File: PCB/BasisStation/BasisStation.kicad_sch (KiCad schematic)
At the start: 17 parts, among them J1 Conn_02x05_Odd_Even, J2 Conn_02x03_Odd_Even, U2 ESP32-S3-WROOM-2

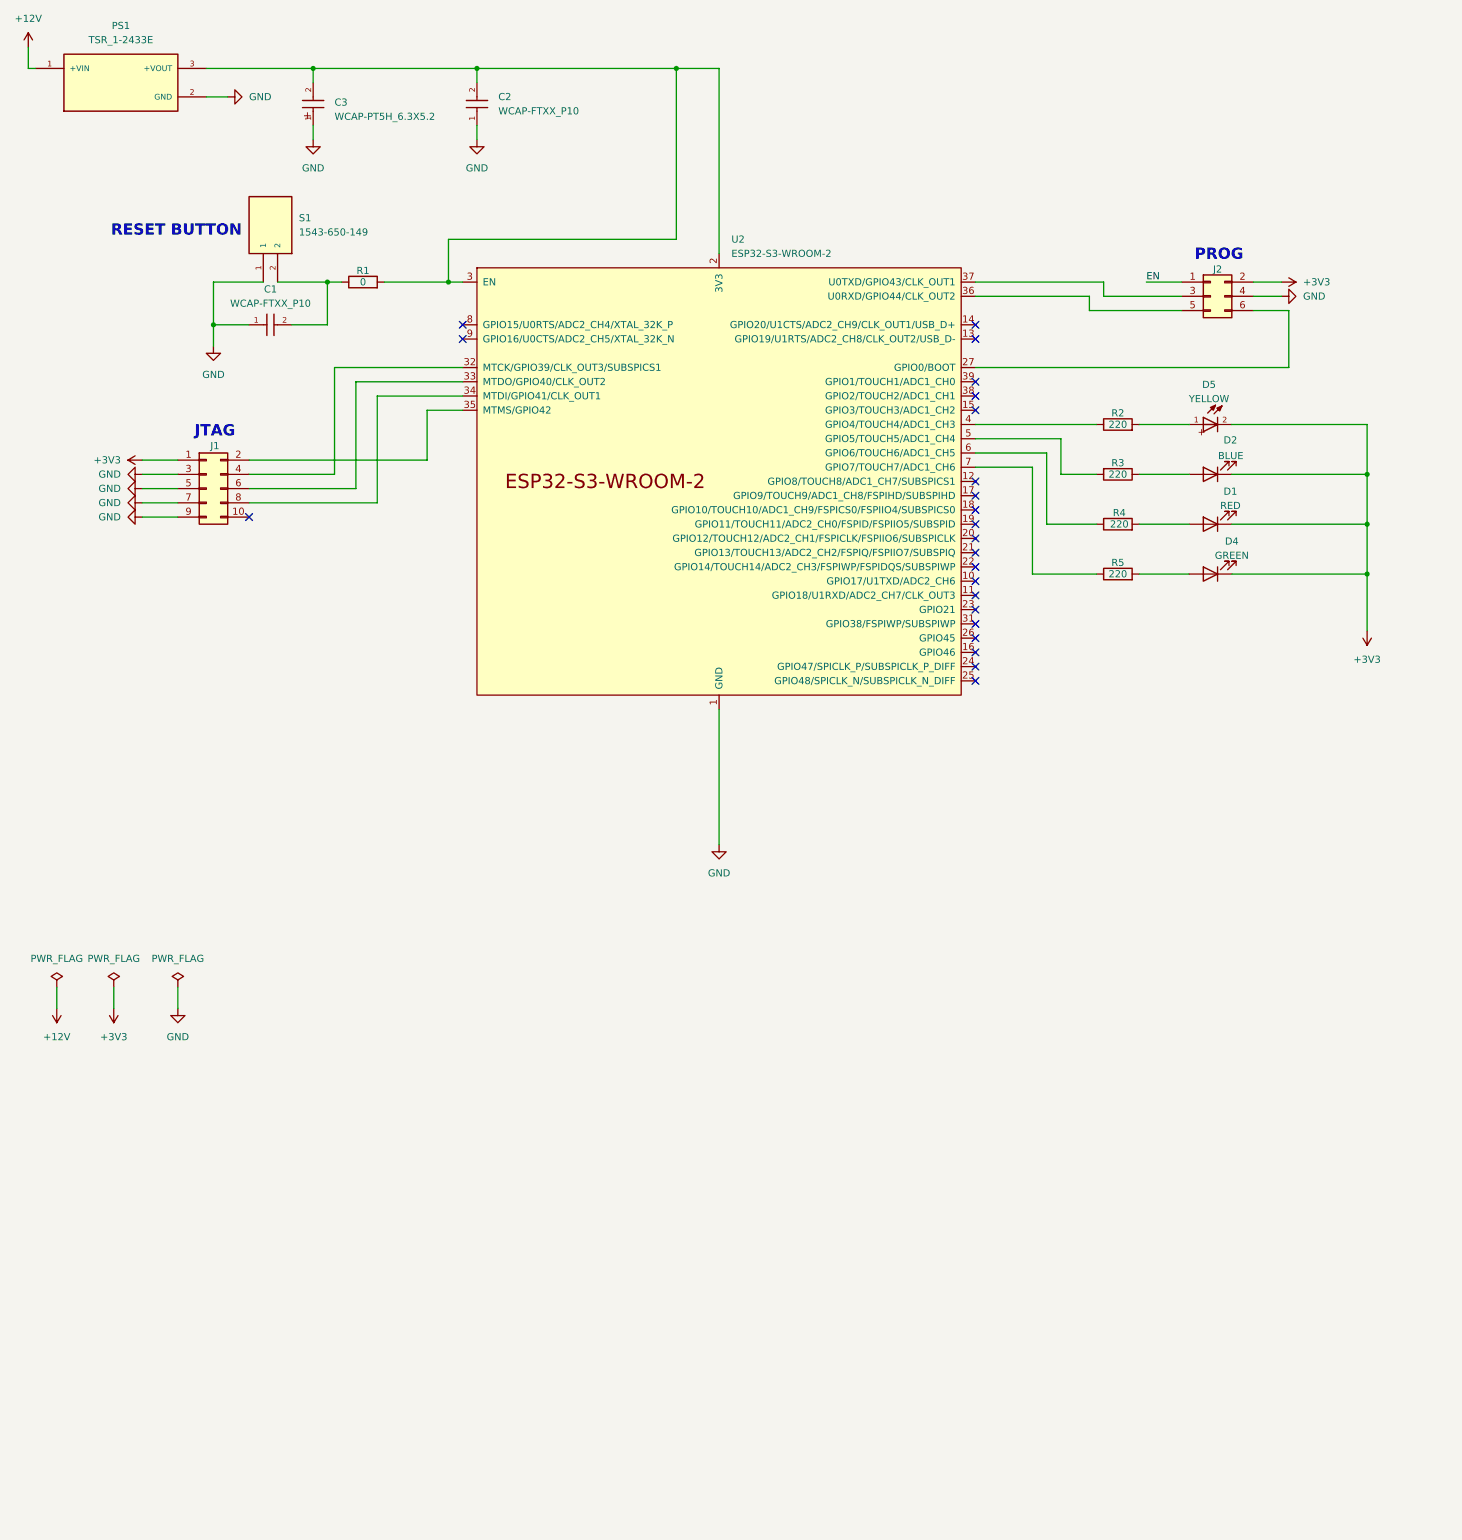
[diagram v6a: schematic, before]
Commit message: microcontroller gewechselt und Layout angepasst
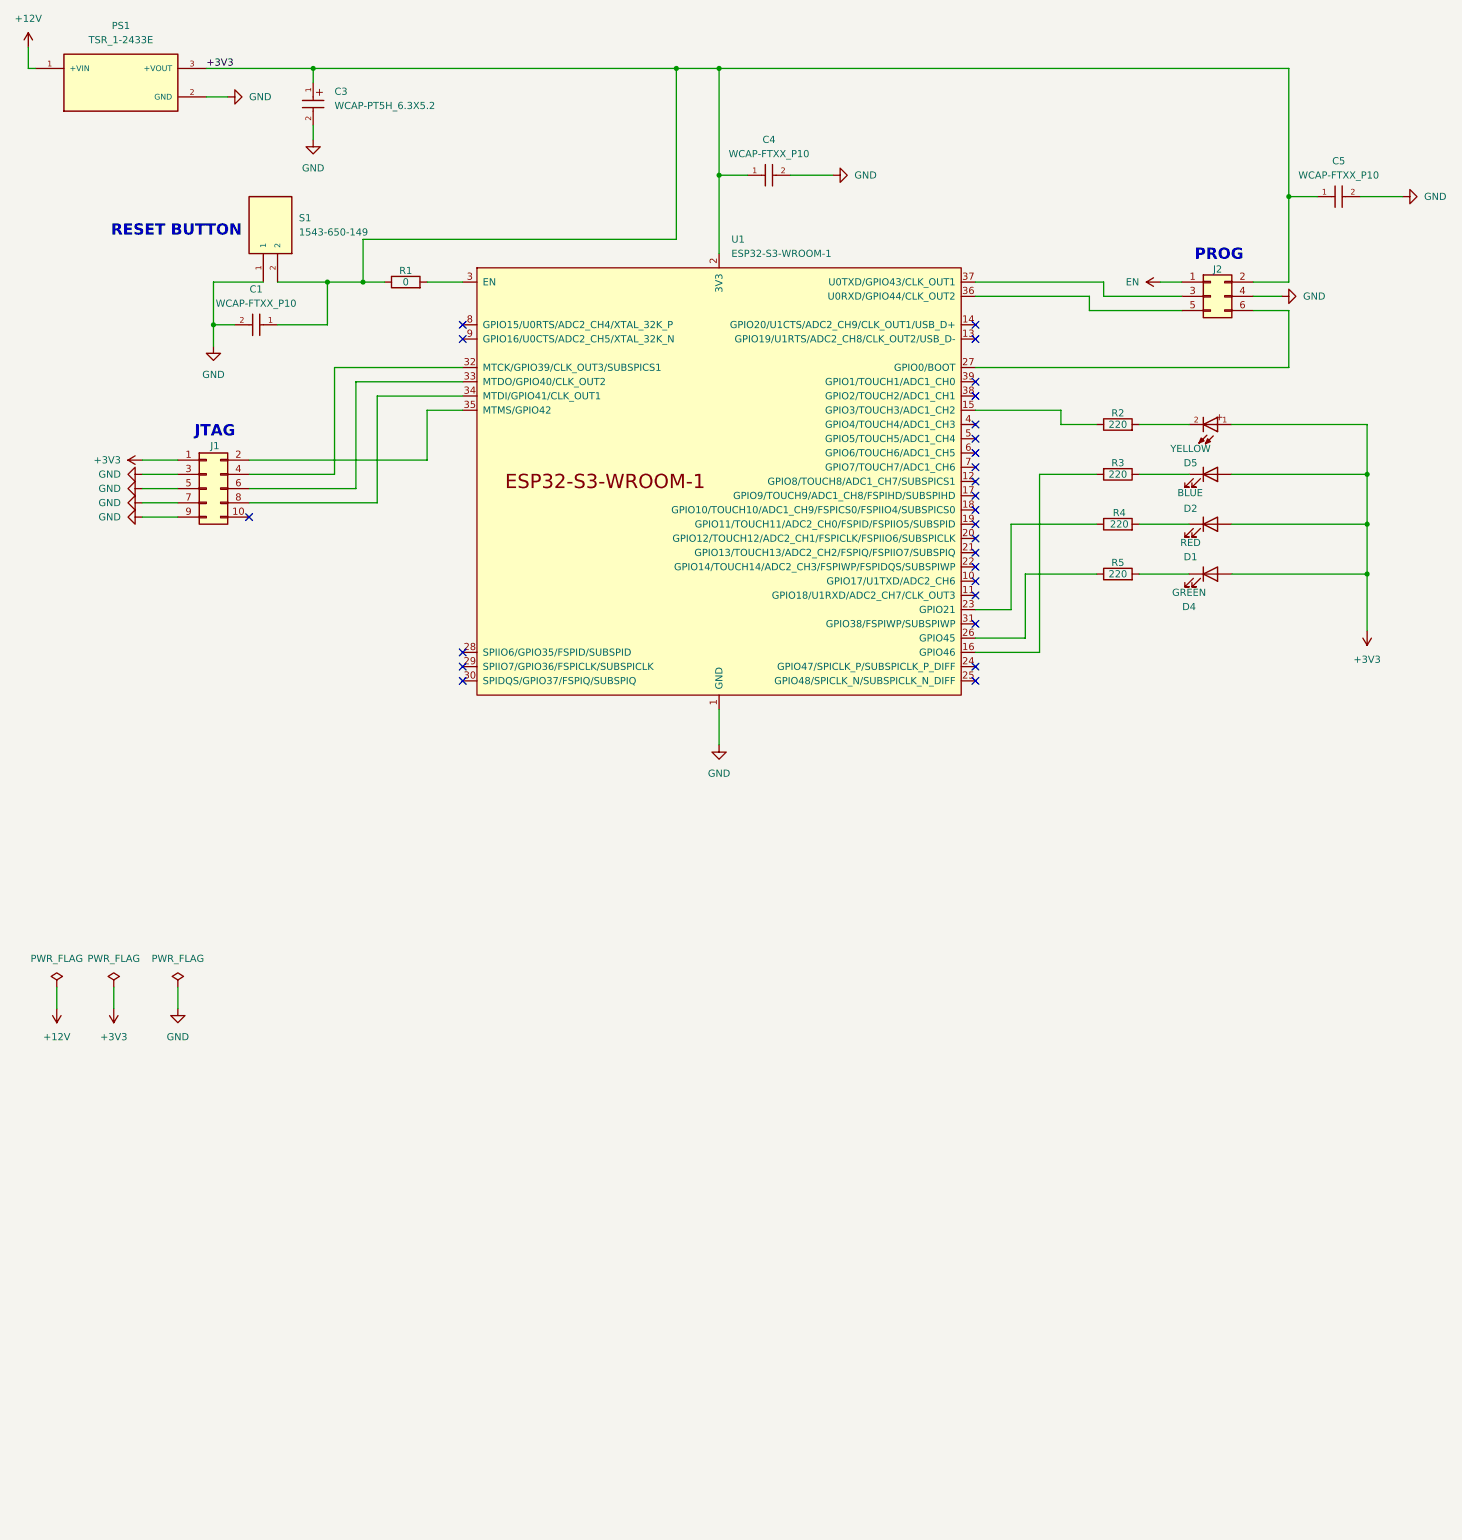
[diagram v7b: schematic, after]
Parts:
- removed C2: WCAP-FTXX_P10, Footprints:WCAP-FTXX_P10L13W7H13, symbol WCAP-FTXX_P10:WCAP-FTXX_P10
- removed U2: ESP32-S3-WROOM-2, Footprints:ESP32-S3-WROOM-2_NEW, symbol PCM_Espressif:ESP32-S3-WROOM-2
- added C4, C5: WCAP-FTXX_P10, Footprints:WCAP-FTXX_P10L13W7H13, symbol WCAP-FTXX_P10:WCAP-FTXX_P10
- added U1: ESP32-S3-WROOM-1, Footprints:ESP32-S3-WROOM-1U, symbol Espressif:ESP32-S3-WROOM-1
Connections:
- net +3V3: now also C1.1, C3.1, D1.2 (A), D2.2 (A), D4.2 (A), D5.1, PS1.3 (+VOUT), R1.1, S1.2, C4.1, C5.1, U1.2 (3V3); no longer D1.1 (K), D2.1 (K), D4.1 (K), D5.2
- net GND: now also C1.2, C3.2, C4.2, C5.2, U1.1 (GND), U1.40 (GND), U1.41 (GND); no longer C1.1, C3.1
- net at R3.1: now also D2.1 (K); no longer D2.2 (A)
- net at R4.1: now also U1.23 (GPIO21)
- net at R4.2: now also D1.1 (K); no longer D1.2 (A)
- net at R5.1: now also U1.26 (GPIO45)
- net at R5.2: now also D4.1 (K); no longer D4.2 (A)
- net at J1.2 (Pin_2): now also U1.35 (MTMS/GPIO42)
- net at J1.4 (Pin_4): now also U1.32 (MTCK/GPIO39/CLK_OUT3/SUBSPICS1)
- net at J1.6 (Pin_6): now also U1.33 (MTDO/GPIO40/CLK_OUT2)
- net at J1.8 (Pin_8): now also U1.34 (MTDI/GPIO41/CLK_OUT1)
- net at J2.6 (Pin_6): now also U1.27 (GPIO0/BOOT)
- net at J2.5 (Pin_5): now also U1.36 (U0RXD/GPIO44/CLK_OUT2)
- net at J2.3 (Pin_3): now also U1.37 (U0TXD/GPIO43/CLK_OUT1)
- net at R2.1: now also U1.15 (GPIO3/TOUCH3/ADC1_CH2)
- net at R3.2: now also U1.16 (GPIO46)
- net at R2.2: now also D5.2; no longer D5.1
- new net: R1.2, U1.3 (EN)
- no-connect marks 23 -> 26
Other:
- moved on the sheet: C1, C3, D1, D2, D4, D5, R1
